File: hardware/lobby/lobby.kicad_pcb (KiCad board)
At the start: 2 copper layers, 27 parts, among them J1 Micro_SD_Card_Det, J2 Conn_01x22_Female, SW1 SW_Push, SW2 SW_SPST, U1 RT9742GGJ5, U2 M.2-keyM, U3 MYLSM00502ERPL, U4 FSUSB42MX

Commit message: sheet refs relative, copied escalator pinout to lobby
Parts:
- moved C1 68.0 mm to (205.8, 79.7)
- moved J1 68.0 mm to (196.0, 88.1)
- moved J2 68.0 mm to (203.7, 140.1)
- moved R6 68.0 mm to (244.2, 83.0)
- moved JP5 68.0 mm to (243.3, 79.9)
- moved R1 68.0 mm to (151.3, 79.4)
- moved C2 68.0 mm to (240.2, 147.2)
- moved C3 68.0 mm to (249.4, 138.0)
- moved JP1 68.0 mm to (247.7, 79.9)
- moved JP2 68.0 mm to (234.0, 89.1)
- moved JP3 68.0 mm to (234.0, 92.7)
- moved JP4 68.0 mm to (238.4, 89.1)
- moved JP6 68.0 mm to (240.0, 85.0)
- moved Module1 68.0 mm to (112.1, 130.3)
- moved R2 68.0 mm to (109.9, 135.8)
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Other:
- copper layers 2 -> 4

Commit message: work abroad
did some light planning for the lobby board while on vacation. now ready for final placement + routing
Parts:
- added C1: 2.2uF, Capacitor_SMD:C_0603_1608Metric, B.Cu at (27.5, 34.5)
- added C10: 2.2uF, Capacitor_SMD:C_0603_1608Metric, F.Cu at (2.49, 63.5)
- added C11: 0.1uF, Capacitor_SMD:C_0603_1608Metric, F.Cu at (6.50, 63.5)
- added C2: 0.1uF, Capacitor_SMD:C_0603_1608Metric, B.Cu at (23.5, 34.5)
- added C4: 2.2uF, Capacitor_SMD:C_0603_1608Metric, B.Cu at (33.0, 70.5)
- added C5: 0.1uF, Capacitor_SMD:C_0603_1608Metric, B.Cu at (37.0, 70.5)
- added C8: 2.2uF, Capacitor_SMD:C_0603_1608Metric, B.Cu at (64.0, 41.5)
- added C9: 0.1uF, Capacitor_SMD:C_0603_1608Metric, B.Cu at (64.0, 43.0)
- added J1: THD-02-R, Connector_PinHeader_2.54mm:PinHeader_2x02_P2.54mm_Vertical, B.Cu at (37.3, 28.3)
- added J2: THD-20-R, Connector_PinHeader_2.54mm:PinHeader_2x20_P2.54mm_Vertical, B.Cu at (89.1, 24.7)
- C3: renamed from C1; footprint Capacitor_SMD:C_0805_2012Metric -> Capacitor_SMD:C_0603_1608Metric
- C6: renamed from C3; footprint Capacitor_SMD:C_0805_2012Metric -> Capacitor_SMD:C_0603_1608Metric
- J3: renamed from J1; moved to B.Cu
- Module2: value cm4-module-A -> hirose-100; footprint cm4crypto:DF40C-100DS-0.4V(51) -> cm4crypto:DF40C-100DP-0.4V(51)
- Module3: value cm4-module-B -> hirose-100; footprint cm4crypto:DF40C-100DS-0.4V(51) -> cm4crypto:DF40C-100DP-0.4V(51)
- R1, R2, U2, U4: moved to B.Cu
- R3, R4: footprint Resistor_SMD:R_0402_1005Metric -> Resistor_SMD:R_0603_1608Metric
- moved U2 261.8 mm to (26.5, 62.5), turned to -90 degrees
- moved J4 194.8 mm to (25.0, 62.5), turned to -90 degrees
- moved Module3 192.0 mm to (22.1, 40.5)
- moved J3 174.4 mm to (27.5, 43.0), turned to -90 degrees
- moved U4 121.1 mm to (64.1, 38.5)
- moved Module2 118.0 mm to (86.0, 62.0)
- moved R2 98.0 mm to (62.5, 50.0), turned to -90 degrees
- moved R1 95.0 mm to (61.0, 50.0), turned to -90 degrees
- moved Module1 76.9 mm to (76.8, 62.0), turned to 90 degrees
- moved C3 26.2 mm to (187.0, 98.0), turned to -90 degrees
- moved R5 24.1 mm to (195.0, 98.5), turned to -90 degrees
- moved R4 20.9 mm to (188.5, 95.0)
- renumbered C2 to C7, J2 to J4, JP5 to JP1, JP1 to JP2, JP2 to JP3, JP3 to JP4, JP4 to JP5, SW2 to SW1, SW1 to SW2
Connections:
- Module1 pad 24: unconnected-(Module1-Pad24) -> /GPIO26
- Module1 pad 25: unconnected-(Module1-Pad25) -> /GPIO21
- Module1 pad 26: unconnected-(Module1-Pad26) -> /GPIO19
- Module1 pad 27: unconnected-(Module1-Pad27) -> /GPIO20
- Module1 pad 28: unconnected-(Module1-Pad28) -> /GPIO13
- Module1 pad 29: unconnected-(Module1-Pad29) -> /GPIO16
- Module1 pad 30: unconnected-(Module1-Pad30) -> /GPIO6
- Module1 pad 31: unconnected-(Module1-Pad31) -> /GPIO12
- Module1 pad 34: unconnected-(Module1-Pad34) -> /GPIO5
- Module1 pad 35: unconnected-(Module1-Pad35) -> /ID_SC
- Module1 pad 36: unconnected-(Module1-Pad36) -> /ID_SD
- Module1 pad 37: unconnected-(Module1-Pad37) -> /GPIO7
- Module1 pad 38: unconnected-(Module1-Pad38) -> /GPIO11
- Module1 pad 39: unconnected-(Module1-Pad39) -> /GPIO8
- Module1 pad 40: unconnected-(Module1-Pad40) -> /GPIO9
- Module1 pad 41: unconnected-(Module1-Pad41) -> /GPIO25
- Module1 pad 44: unconnected-(Module1-Pad44) -> /GPIO10
- Module1 pad 45: unconnected-(Module1-Pad45) -> /GPIO24
- Module1 pad 46: unconnected-(Module1-Pad46) -> /GPIO22
- Module1 pad 47: unconnected-(Module1-Pad47) -> /GPIO23
- Module1 pad 48: unconnected-(Module1-Pad48) -> /GPIO27
- Module1 pad 49: unconnected-(Module1-Pad49) -> /GPIO18
- Module1 pad 50: unconnected-(Module1-Pad50) -> /GPIO17
- Module1 pad 51: unconnected-(Module1-Pad51) -> /GPIO15
- Module1 pad 55: unconnected-(Module1-Pad55) -> /GPIO14
- Module2 pad 10: /TRD0_N -> /TRD3_P
- Module2 pad 100: unconnected-(Module2-Pad100) -> GND
- Module2 pad 11: /TRD2_P -> /TRD1_N
- Module2 pad 12: /TRD0_P -> /TRD3_N
- Module2 pad 15: /ETH_LEDY -> /TR1_TAP
- Module2 pad 16: unconnected-(Module2-Pad16) -> /TR3_TAP
- Module2 pad 17: /ETH_LEDG -> /TR1_TAP
- Module2 pad 18: unconnected-(Module2-Pad18) -> /TR3_TAP
- Module2 pad 19: unconnected-(Module2-Pad19) -> /TR1_TAP
- Module2 pad 20: unconnected-(Module2-Pad20) -> /TR3_TAP
- Module2 pad 21: /nPI_LED_ACTIVITY -> GND
- Module2 pad 23: GND -> /TR2_TAP
- Module2 pad 24: unconnected-(Module2-Pad24) -> /TR0_TAP
- Module2 pad 25: unconnected-(Module2-Pad25) -> /TR2_TAP
- Module2 pad 26: unconnected-(Module2-Pad26) -> /TR0_TAP
- Module2 pad 27: unconnected-(Module2-Pad27) -> /TR2_TAP
- Module2 pad 28: unconnected-(Module2-Pad28) -> /TR0_TAP
- Module2 pad 29: unconnected-(Module2-Pad29) -> GND
- Module2 pad 3: /TRD3_P -> /TRD0_N
- Module2 pad 30: unconnected-(Module2-Pad30) -> GND
- Module2 pad 31: unconnected-(Module2-Pad31) -> /+5v
- Module2 pad 32: GND -> /+5v
- Module2 pad 33: GND -> /+5v
- Module2 pad 34: unconnected-(Module2-Pad34) -> /+5v
- Module2 pad 35: unconnected-(Module2-Pad35) -> /+5v
- Module2 pad 36: unconnected-(Module2-Pad36) -> /+5v
- Module2 pad 37: unconnected-(Module2-Pad37) -> /+5v
- Module2 pad 38: unconnected-(Module2-Pad38) -> /+5v
- Module2 pad 39: unconnected-(Module2-Pad39) -> /+5v
- Module2 pad 4: /TRD1_P -> /TRD2_P
- Module2 pad 40: unconnected-(Module2-Pad40) -> /+5v
- Module2 pad 41: unconnected-(Module2-Pad41) -> /+5v
- Module2 pad 42: GND -> /+5v
- Module2 pad 43: GND -> /+5v
- Module2 pad 44: unconnected-(Module2-Pad44) -> /+5v
- Module2 pad 45: unconnected-(Module2-Pad45) -> GND
- Module2 pad 46: unconnected-(Module2-Pad46) -> GND
- Module2 pad 47: unconnected-(Module2-Pad47) -> GND
- Module2 pad 48: unconnected-(Module2-Pad48) -> /+3.3v
- Module2 pad 49: unconnected-(Module2-Pad49) -> /AnalogIP1
- Module2 pad 5: /TRD3_N -> /TRD0_P
- Module2 pad 50: unconnected-(Module2-Pad50) -> /+3.3v
- Module2 pad 51: unconnected-(Module2-Pad51) -> /AnalogIP0
- Module2 pad 54: /GPIO4 -> /ETH_LEDY
- Module2 pad 55: unconnected-(Module2-Pad55) -> /USB2_HOST_P
- Module2 pad 56: /GPIO3 -> /ETH_LEDG
- Module2 pad 57: unconnected-(Module2-Pad57) -> /USB2_HOST_N
- Module2 pad 58: /GPIO2 -> /nPI_LED_ACTIVITY
- Module2 pad 6: /TRD1_N -> /TRD2_N
- Module2 pad 60: GND -> /nPI_LED_PWR
- Module2 pad 61: unconnected-(Module2-Pad61) -> /USB2_DEV_N
- Module2 pad 62: unconnected-(Module2-Pad62) -> GND
- Module2 pad 63: unconnected-(Module2-Pad63) -> /USB2_DEV_P
- Module2 pad 64: unconnected-(Module2-Pad64) -> GND
- Module2 pad 67: unconnected-(Module2-Pad67) -> /HDMI1_HOTPLUG
- Module2 pad 68: unconnected-(Module2-Pad68) -> /HDMI0_HOTPLUG
- Module2 pad 69: unconnected-(Module2-Pad69) -> /HDMI1_CEC
- Module2 pad 70: unconnected-(Module2-Pad70) -> /HDMI0_CEC
- Module2 pad 71: GND -> /HDMI1_SDA
- Module2 pad 72: unconnected-(Module2-Pad72) -> /HDMI0_SDA
- Module2 pad 73: unconnected-(Module2-Pad73) -> /HDMI1_SCL
- Module2 pad 74: GND -> /HDMI0_SCL
- Module2 pad 75: unconnected-(Module2-Pad75) -> GND
- Module2 pad 76: unconnected-(Module2-Pad76) -> GND
- Module2 pad 77: /+5v -> /HDMI1_TX0_P
- Module2 pad 78: unconnected-(Module2-Pad78) -> /HDMI0_TX0_N
- Module2 pad 79: /+5v -> /HDMI1_TX0_N
- Module2 pad 80: unconnected-(Module2-Pad80) -> /HDMI0_TX0_P
- Module2 pad 81: /+5v -> GND
- Module2 pad 82: unconnected-(Module2-Pad82) -> GND
- Module2 pad 83: /+5v -> /HDMI1_TX2_P
- Module2 pad 84: /+3.3v -> /HDMI0_TX2_N
- Module2 pad 85: /+5v -> /HDMI1_TX2_N
- Module2 pad 86: /+3.3v -> /HDMI0_TX2_P
- Module2 pad 87: /+5v -> GND
- Module2 pad 88: /+1.8v -> GND
- Module2 pad 89: unconnected-(Module2-Pad89) -> /HDMI0_TX1_P
- Module2 pad 9: /TRD2_N -> /TRD1_P
- Module2 pad 90: /+1.8v -> /HDMI1_CLK_N
- Module2 pad 91: unconnected-(Module2-Pad91) -> /HDMI0_TX1_N
- Module2 pad 92: unconnected-(Module2-Pad92) -> /HDMI1_CLK_P
- Module2 pad 93: unconnected-(Module2-Pad93) -> GND
- Module2 pad 94: /AnalogIP1 -> GND
- Module2 pad 95: /nPI_LED_PWR -> /HDMI0_CLK_P
- Module2 pad 96: /AnalogIP0 -> /HDMI1_TX1_N
- Module2 pad 97: unconnected-(Module2-Pad97) -> /HDMI0_CLK_N
- Module2 pad 98: GND -> /HDMI1_TX1_P
- Module2 pad 99: unconnected-(Module2-Pad99) -> GND
- Module3 pad 100: /HDMI0_SCL -> unconnected-(Module3-Pad100)
- Module3 pad 13: GND -> unconnected-(Module3-Pad13)
- Module3 pad 14: GND -> unconnected-(Module3-Pad14)
- Module3 pad 19: GND -> unconnected-(Module3-Pad19)
- Module3 pad 20: GND -> unconnected-(Module3-Pad20)
- Module3 pad 25: GND -> unconnected-(Module3-Pad25)
- Module3 pad 26: GND -> unconnected-(Module3-Pad26)
- Module3 pad 3: /USB2_HOST_N -> unconnected-(Module3-Pad3)
- Module3 pad 31: GND -> unconnected-(Module3-Pad31)
- Module3 pad 32: GND -> unconnected-(Module3-Pad32)
- Module3 pad 37: GND -> unconnected-(Module3-Pad37)
- Module3 pad 38: GND -> unconnected-(Module3-Pad38)
- Module3 pad 43: /HDMI1_HOTPLUG -> unconnected-(Module3-Pad43)
- Module3 pad 44: GND -> unconnected-(Module3-Pad44)
- Module3 pad 45: /HDMI1_SDA -> unconnected-(Module3-Pad45)
- Module3 pad 46: /HDMI1_TX2_P -> unconnected-(Module3-Pad46)
- Module3 pad 47: /HDMI1_SCL -> unconnected-(Module3-Pad47)
- Module3 pad 48: /HDMI1_TX2_N -> unconnected-(Module3-Pad48)
- Module3 pad 49: /HDMI1_CEC -> unconnected-(Module3-Pad49)
- Module3 pad 5: /USB2_HOST_P -> unconnected-(Module3-Pad5)
- Module3 pad 50: GND -> unconnected-(Module3-Pad50)
- Module3 pad 51: /HDMI0_CEC -> unconnected-(Module3-Pad51)
- Module3 pad 52: /HDMI1_TX1_P -> unconnected-(Module3-Pad52)
- Module3 pad 53: /HDMI0_HOTPLUG -> unconnected-(Module3-Pad53)
- Module3 pad 54: /HDMI1_TX1_N -> unconnected-(Module3-Pad54)
- Module3 pad 55: GND -> unconnected-(Module3-Pad55)
- Module3 pad 56: GND -> unconnected-(Module3-Pad56)
- Module3 pad 58: /HDMI1_TX0_P -> unconnected-(Module3-Pad58)
- Module3 pad 60: /HDMI1_TX0_N -> unconnected-(Module3-Pad60)
- Module3 pad 61: GND -> unconnected-(Module3-Pad61)
- Module3 pad 62: GND -> unconnected-(Module3-Pad62)
- Module3 pad 64: /HDMI1_CLK_P -> unconnected-(Module3-Pad64)
- Module3 pad 66: /HDMI1_CLK_N -> unconnected-(Module3-Pad66)
- Module3 pad 67: GND -> unconnected-(Module3-Pad67)
- Module3 pad 68: GND -> unconnected-(Module3-Pad68)
- Module3 pad 7: GND -> unconnected-(Module3-Pad7)
- Module3 pad 70: /HDMI0_TX2_P -> unconnected-(Module3-Pad70)
- Module3 pad 72: /HDMI0_TX2_N -> unconnected-(Module3-Pad72)
- Module3 pad 73: GND -> unconnected-(Module3-Pad73)
- Module3 pad 74: GND -> unconnected-(Module3-Pad74)
- Module3 pad 76: /HDMI0_TX1_P -> unconnected-(Module3-Pad76)
- Module3 pad 78: /HDMI0_TX1_N -> unconnected-(Module3-Pad78)
- Module3 pad 79: GND -> unconnected-(Module3-Pad79)
- Module3 pad 8: GND -> unconnected-(Module3-Pad8)
- Module3 pad 80: GND -> unconnected-(Module3-Pad80)
- Module3 pad 82: /HDMI0_TX0_P -> unconnected-(Module3-Pad82)
- Module3 pad 84: /HDMI0_TX0_N -> unconnected-(Module3-Pad84)
- Module3 pad 85: GND -> unconnected-(Module3-Pad85)
- Module3 pad 86: GND -> unconnected-(Module3-Pad86)
- Module3 pad 88: /HDMI0_CLK_P -> unconnected-(Module3-Pad88)
- Module3 pad 90: /HDMI0_CLK_N -> unconnected-(Module3-Pad90)
- Module3 pad 91: GND -> unconnected-(Module3-Pad91)
- Module3 pad 92: GND -> unconnected-(Module3-Pad92)
- Module3 pad 93: /USB2_DEV_N -> unconnected-(Module3-Pad93)
- Module3 pad 95: /USB2_DEV_P -> unconnected-(Module3-Pad95)
- Module3 pad 97: GND -> unconnected-(Module3-Pad97)
- Module3 pad 98: GND -> unconnected-(Module3-Pad98)
- Module3 pad 99: /HDMI0_SDA -> unconnected-(Module3-Pad99)
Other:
- board outline added: 85 x 56 mm

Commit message: place lobby components
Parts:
- removed the JP1 at (243.3, 79.9)
- removed JP6: SolderJumper_2_Open, Jumper:SolderJumper-2_P1.3mm_Open_TrianglePad1.0x1.5mm
- added JP5: Jumper_3_Bridged12, Jumper:SolderJumper-3_P1.3mm_Bridged12_RoundedPad1.0x1.5mm, B.Cu at (56.2, 37.5)
- C1: renamed from C3; moved to B.Cu
- C10, C11, R3, R4, R6, R7, U1, U3: moved to B.Cu
- C6: renamed from C7; moved to B.Cu
- C7: renamed from C6; moved to B.Cu
- JP1: renamed from JP2; footprint Jumper:SolderJumper-2_P1.3mm_Open_TrianglePad1.0x1.5mm -> Jumper:SolderJumper-2_P1.3mm_Open_RoundedPad1.0x1.5mm; moved to B.Cu
- JP2: renamed from JP3; footprint Jumper:SolderJumper-2_P1.3mm_Open_TrianglePad1.0x1.5mm -> Jumper:SolderJumper-2_P1.3mm_Open_RoundedPad1.0x1.5mm; moved to B.Cu
- JP3: renamed from JP4; footprint Jumper:SolderJumper-2_P1.3mm_Open_TrianglePad1.0x1.5mm -> Jumper:SolderJumper-2_P1.3mm_Open_RoundedPad1.0x1.5mm; moved to B.Cu
- JP4: renamed from JP5; footprint Jumper:SolderJumper-2_P1.3mm_Open_TrianglePad1.0x1.5mm -> Jumper:SolderJumper-2_P1.3mm_Open_RoundedPad1.0x1.5mm; moved to B.Cu
- R5: footprint Resistor_SMD:R_0402_1005Metric -> Resistor_SMD:R_0603_1608Metric; moved to B.Cu
- SW1: renamed from SW2; moved to B.Cu
- SW2: renamed from SW1; moved to B.Cu
- moved R6 225.2 mm to (25.0, 31.5), turned to 90 degrees
- moved SW2 220.7 mm to (21.5, 31.5), turned to 90 degrees
- moved C7 206.7 mm to (68.0, 39.0), turned to 90 degrees
- moved R7 203.2 mm to (69.8, 39.0), turned to 90 degrees
- moved C6 200.2 mm to (71.8, 39.0), turned to 90 degrees
- moved JP1 193.6 mm to (56.3, 51.0), turned to 180 degrees
- moved U3 190.8 mm to (73.8, 49.2), turned to 180 degrees
- moved JP4 188.1 mm to (56.3, 42.0), turned to 180 degrees
- moved JP3 184.0 mm to (56.3, 45.0), turned to 180 degrees
- moved JP2 182.4 mm to (56.3, 48.0), turned to 180 degrees
- moved SW1 181.3 mm to (56.2, 54.2)
- moved R5 144.0 mm to (62.0, 43.2), turned to 0 degrees
- moved U1 141.6 mm to (62.0, 40.1), turned to -90 degrees
- moved C1 139.1 mm to (62.0, 37.0), turned to 0 degrees
- moved R3 139.1 mm to (62.0, 47.0), turned to 180 degrees
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- renumbered C1 to C2, C2 to C3
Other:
- outline, holes or cut-outs redrawn

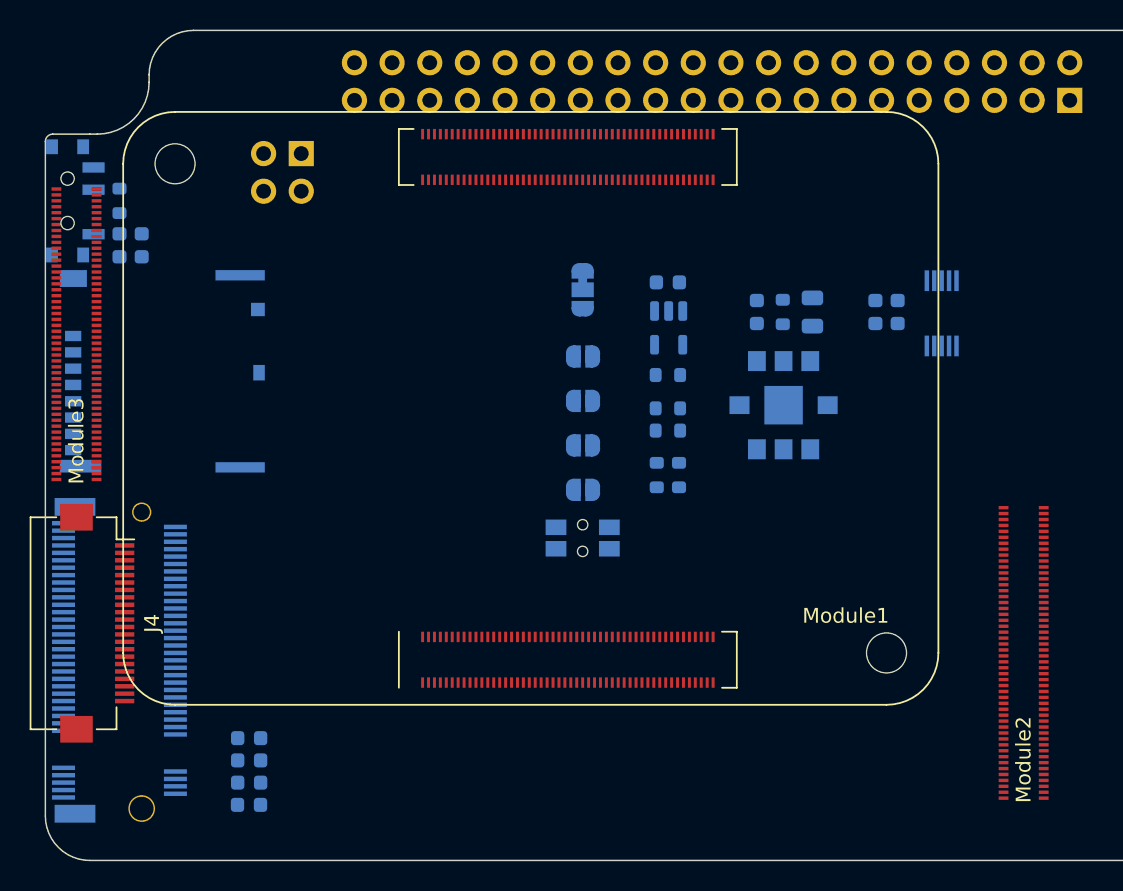
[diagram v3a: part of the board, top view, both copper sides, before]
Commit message: attempt to route gpio
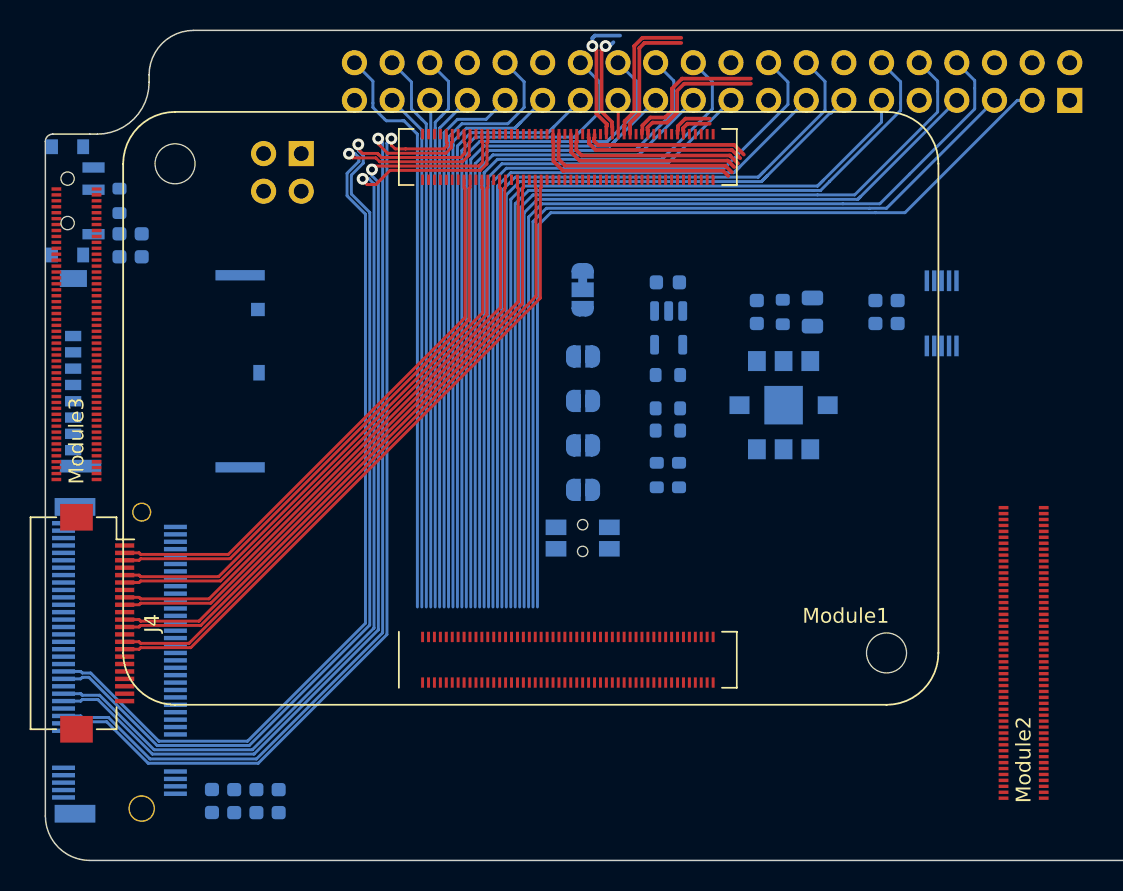
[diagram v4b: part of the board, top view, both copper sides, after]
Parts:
- moved C10 4.69 mm to (35.7, 72.0), turned to -90 degrees
- moved C4 2.79 mm to (34.2, 72.0), turned to -90 degrees
- moved C11 2.51 mm to (31.2, 72.0), turned to -90 degrees
- moved C5 1.61 mm to (32.7, 72.0), turned to -90 degrees
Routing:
- net /PCIE_RX_P: track 0.00 -> 68.7 mm, vias 0 -> 1
- net /PCIE_RX_N: track 0.00 -> 68.7 mm, vias 0 -> 1
- net /PCIE_TX_N: track 0.00 -> 68.6 mm, vias 0 -> 1
- net /PCIE_TX_P: track 0.00 -> 67.1 mm, vias 0 -> 1
- net /PCIE_CLK_N: track 0.00 -> 66.4 mm, vias 0 -> 1
- net /PCIE_CLK_P: track 0.00 -> 65.4 mm, vias 0 -> 1
- net /GPIO14: track 0.00 -> 63.0 mm
- net /GPIO2: track 0.00 -> 62.6 mm
- net /GPIO15: track 0.00 -> 61.6 mm
- net /GPIO3: track 0.00 -> 60.5 mm
- net /GPIO18: track 0.00 -> 59.6 mm
- net /GPIO4: track 0.00 -> 59.2 mm
- net /GPIO17: track 0.00 -> 56.7 mm
- net /GPIO23: track 0.00 -> 56.4 mm
- net /GPIO24: track 0.00 -> 54.7 mm
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
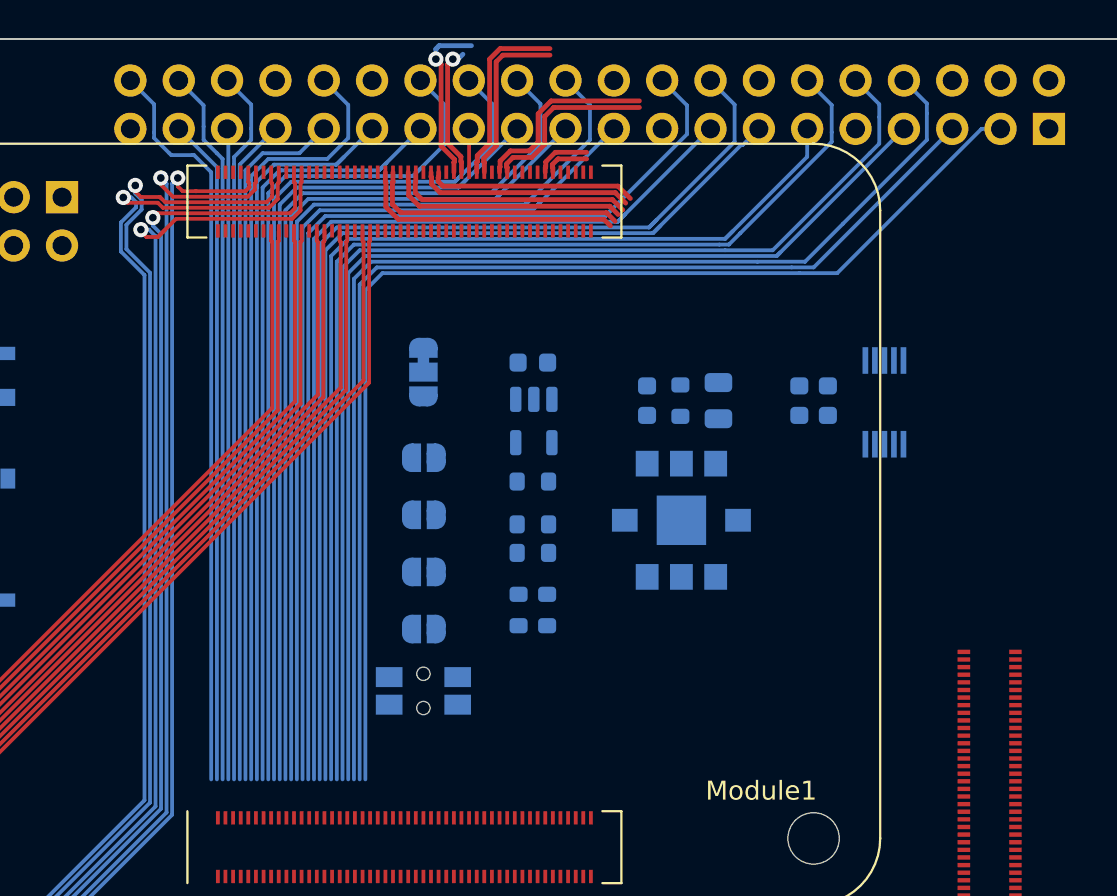
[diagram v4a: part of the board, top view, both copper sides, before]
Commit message: removed gpio from lobby to simplify routing
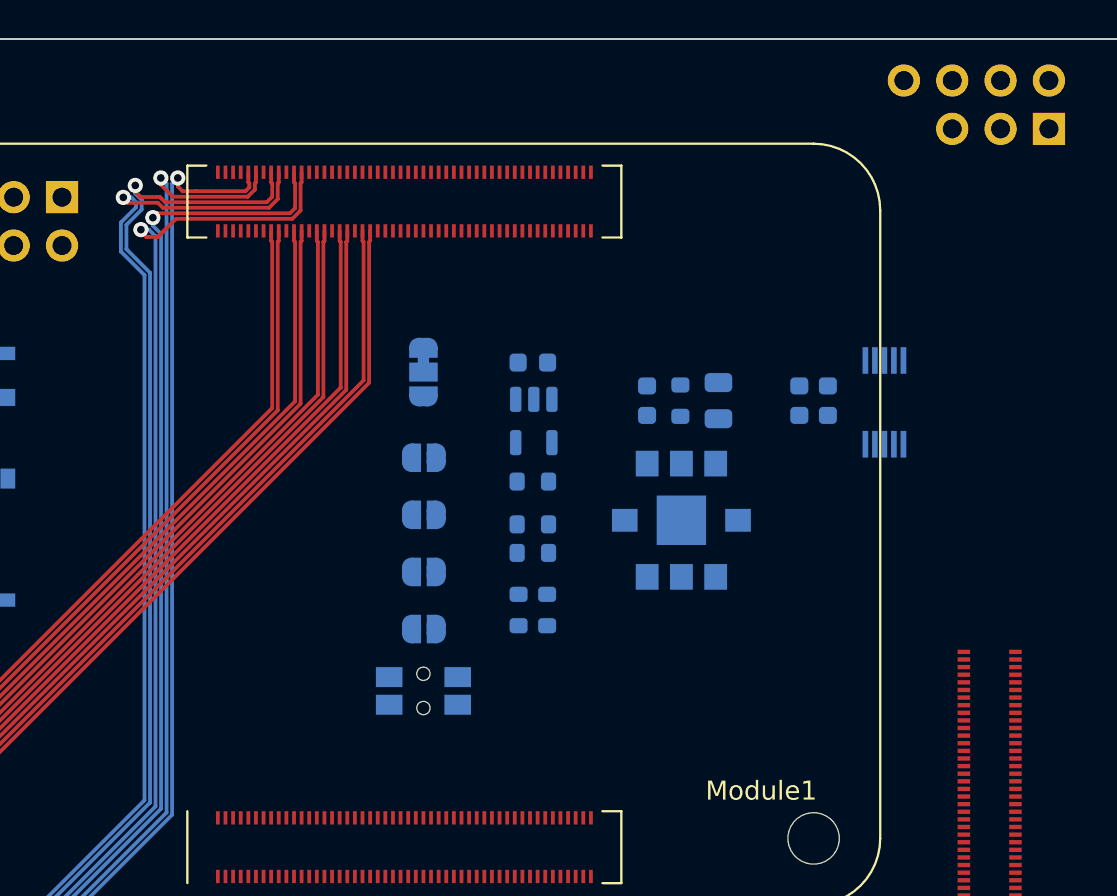
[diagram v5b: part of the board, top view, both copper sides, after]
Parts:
- J2: footprint Connector_PinHeader_2.54mm:PinHeader_2x20_P2.54mm_Vertical -> cm4crypto:rpi-40-just-power
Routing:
- net /GPIO14: track 63.0 -> 0.00 mm
- net /GPIO2: track 62.6 -> 0.00 mm
- net /GPIO15: track 61.6 -> 0.00 mm
- net /GPIO3: track 60.5 -> 0.00 mm
- net /GPIO18: track 59.6 -> 0.00 mm
- net /GPIO4: track 59.2 -> 0.00 mm
- net /GPIO17: track 56.7 -> 0.00 mm
- net /GPIO23: track 56.4 -> 0.00 mm
- net /GPIO24: track 54.7 -> 0.00 mm
- net /GPIO27: track 53.8 -> 0.00 mm
- net /GPIO22: track 52.2 -> 0.00 mm
- net /GPIO25: track 50.7 -> 0.00 mm
- net /GPIO8: track 49.1 -> 0.00 mm
- net /GPIO10: track 48.1 -> 0.00 mm
- net /GPIO7: track 47.6 -> 0.00 mm
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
